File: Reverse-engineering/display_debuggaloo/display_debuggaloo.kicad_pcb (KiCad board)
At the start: 2 copper layers, 24.1 x 30.5 mm, 5 parts, among them J1 COMM, J2 DBG, J3 VCC, J4 VCC

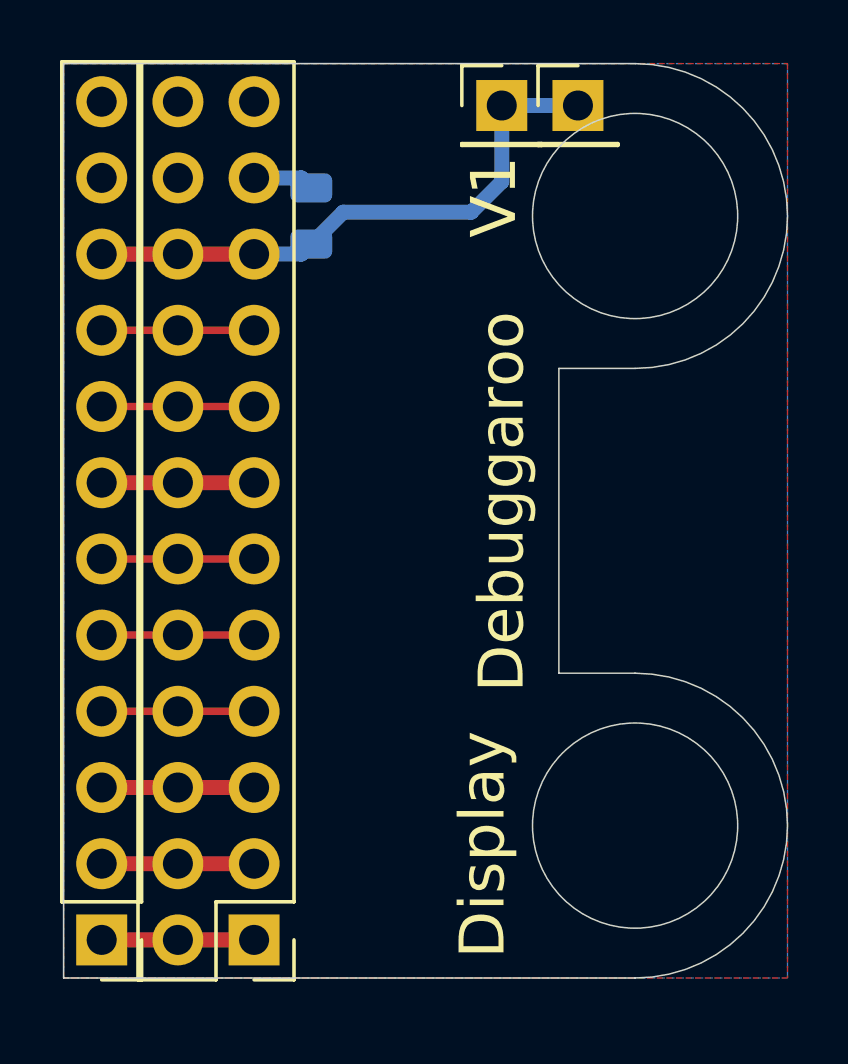
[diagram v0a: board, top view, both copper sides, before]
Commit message: display_debuggaloo: updating to kicad 7
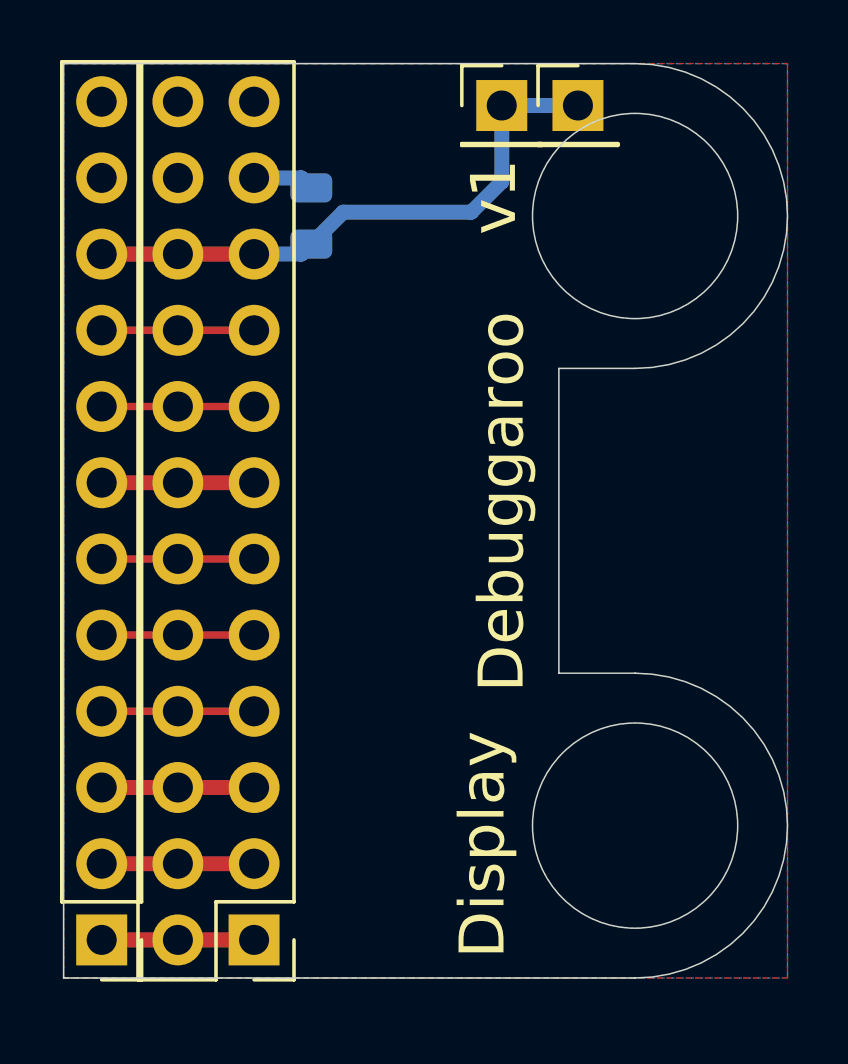
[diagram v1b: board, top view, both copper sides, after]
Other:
- net class Default removed
- rule pad_to_mask_clearance: 0.051 -> 0
- board text added: "v1"
- board text added: "v1 by Arya"
- board text removed: "V1"
- board text removed: "V1 by CRImier"
